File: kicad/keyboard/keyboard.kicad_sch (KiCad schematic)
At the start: 101 parts, among them U3 ATmega328-P, Y1 Crystal

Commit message: Dual support for ASM & C programs. Took some time!
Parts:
- added R1: 5K, Resistor_THT:R_Axial_DIN0204_L3.6mm_D1.6mm_P2.54mm_Vertical, symbol Device:R
- renumbered C4 to C1, C4 to C2, C4 to C3, KD1 to D1, KD10 to D10, KD11 to D11, KD12 to D12, KD13 to D13, KD14 to D14, KD15 to D15, KD16 to D16, KD17 to D17, KD18 to D18, KD19 to D19, KD2 to D2, KD20 to D20, KD21 to D21, KD22 to D22, KD23 to D23, KD24 to D24, KD25 to D25, KD26 to D26, KD27 to D27, KD28 to D28, KD29 to D29, KD3 to D3, KD30 to D30, KD31 to D31, KD32 to D32, KD33 to D33, KD34 to D34, KD35 to D35, KD36 to D36, KD37 to D37, KD38 to D38, KD39 to D39, KD4 to D4, KD40 to D40, KD41 to D41, KD42 to D42, KD43 to D43, KD44 to D44, KD45 to D45, KD46 to D46, KD47 to D47, KD48 to D48, KD5 to D5, KD6 to D6, KD7 to D7, KD8 to D8, KD9 to D9, KSW1 to SW1, KSW10 to SW10, KSW11 to SW11, KSW12 to SW12, KSW13 to SW13, KSW14 to SW14, KSW15 to SW15, KSW16 to SW16, KSW17 to SW17, KSW18 to SW18, KSW19 to SW19, KSW2 to SW2, KSW20 to SW20, KSW21 to SW21, KSW22 to SW22, KSW23 to SW23, KSW24 to SW24, KSW25 to SW25, KSW26 to SW26, KSW27 to SW27, KSW28 to SW28, KSW29 to SW29, KSW3 to SW3, KSW30 to SW30, KSW31 to SW31, KSW32 to SW32, KSW33 to SW33, KSW34 to SW34, KSW35 to SW35, KSW36 to SW36, KSW37 to SW37, KSW38 to SW38, KSW39 to SW39, KSW4 to SW4, KSW40 to SW40, KSW41 to SW41, KSW42 to SW42, KSW43 to SW43, KSW44 to SW44, KSW45 to SW45, KSW46 to SW46, KSW47 to SW47, KSW48 to SW48, KSW5 to SW5, KSW6 to SW6, KSW7 to SW7, KSW8 to SW8, KSW9 to SW9
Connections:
- net +5V: now also R1.2
- net ~{RES}: no longer names the net of U3.1 (~{RESET}/PC6)
- net ~{RES}: now also R1.1

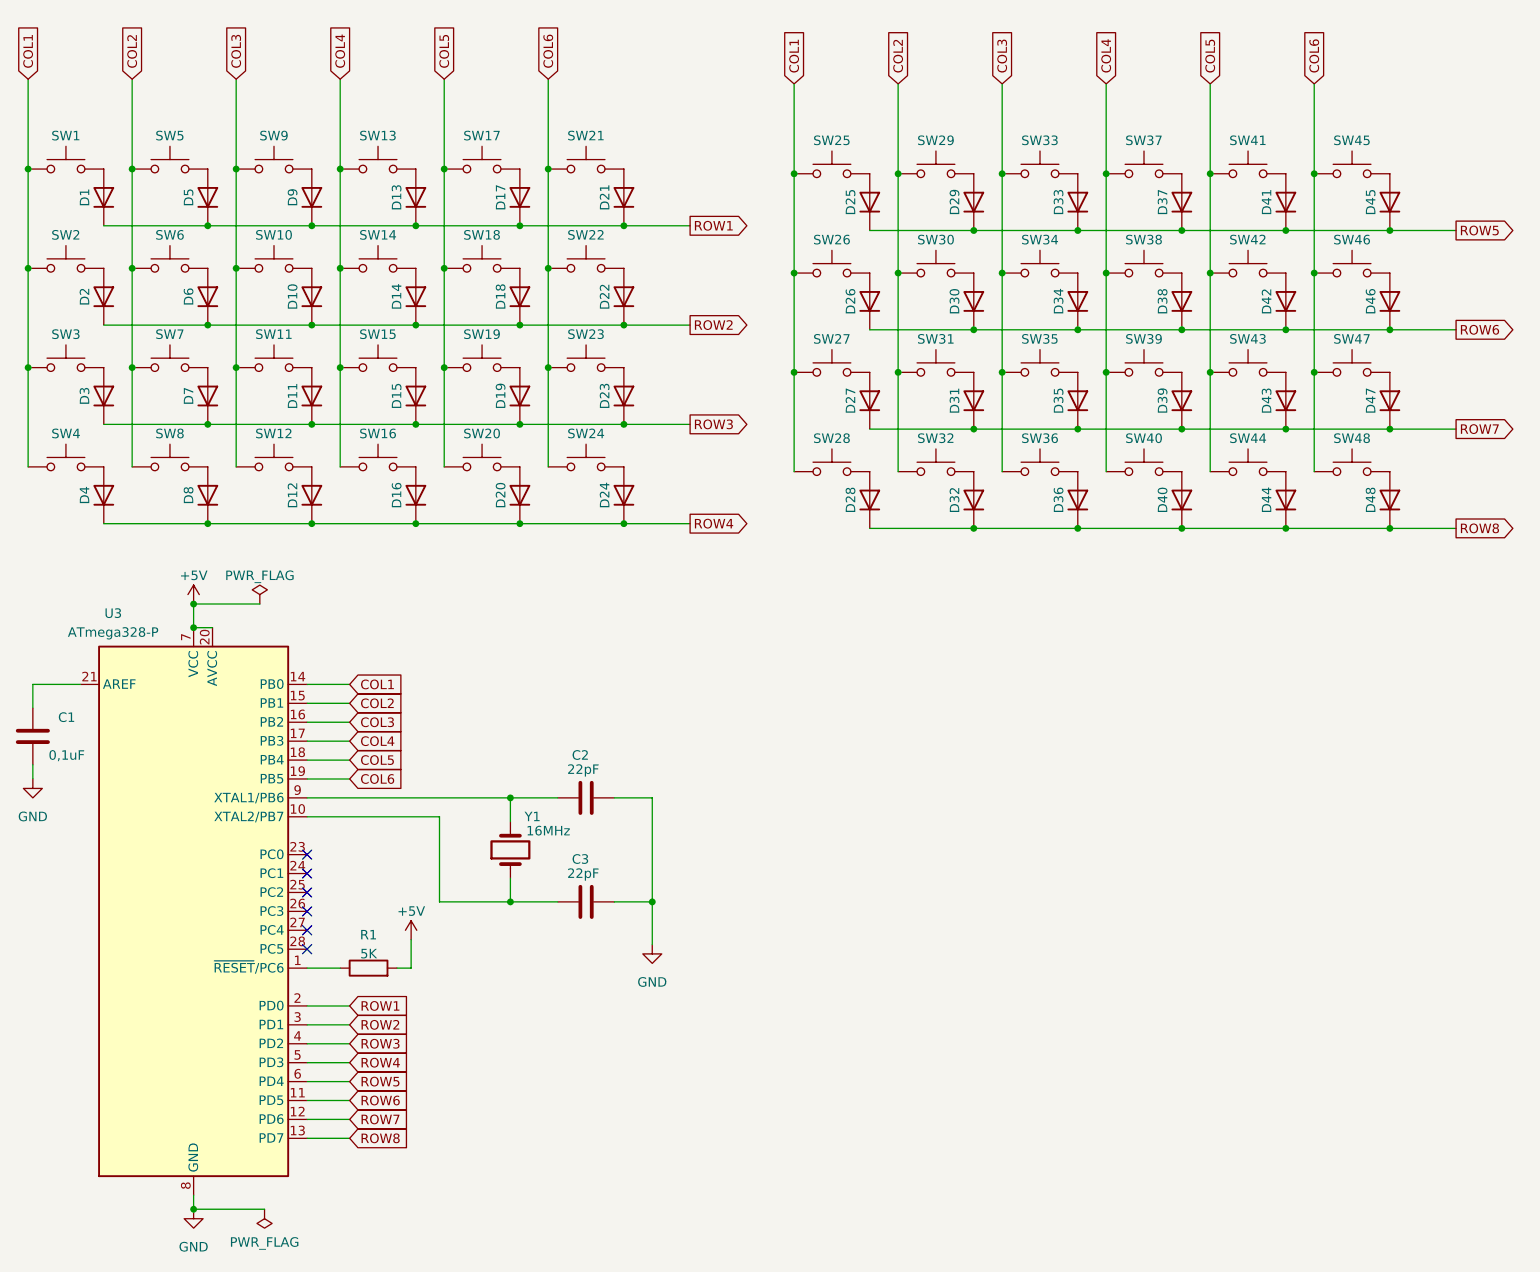
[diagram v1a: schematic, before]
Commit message: Load large files from FAT16, WIP for Maze
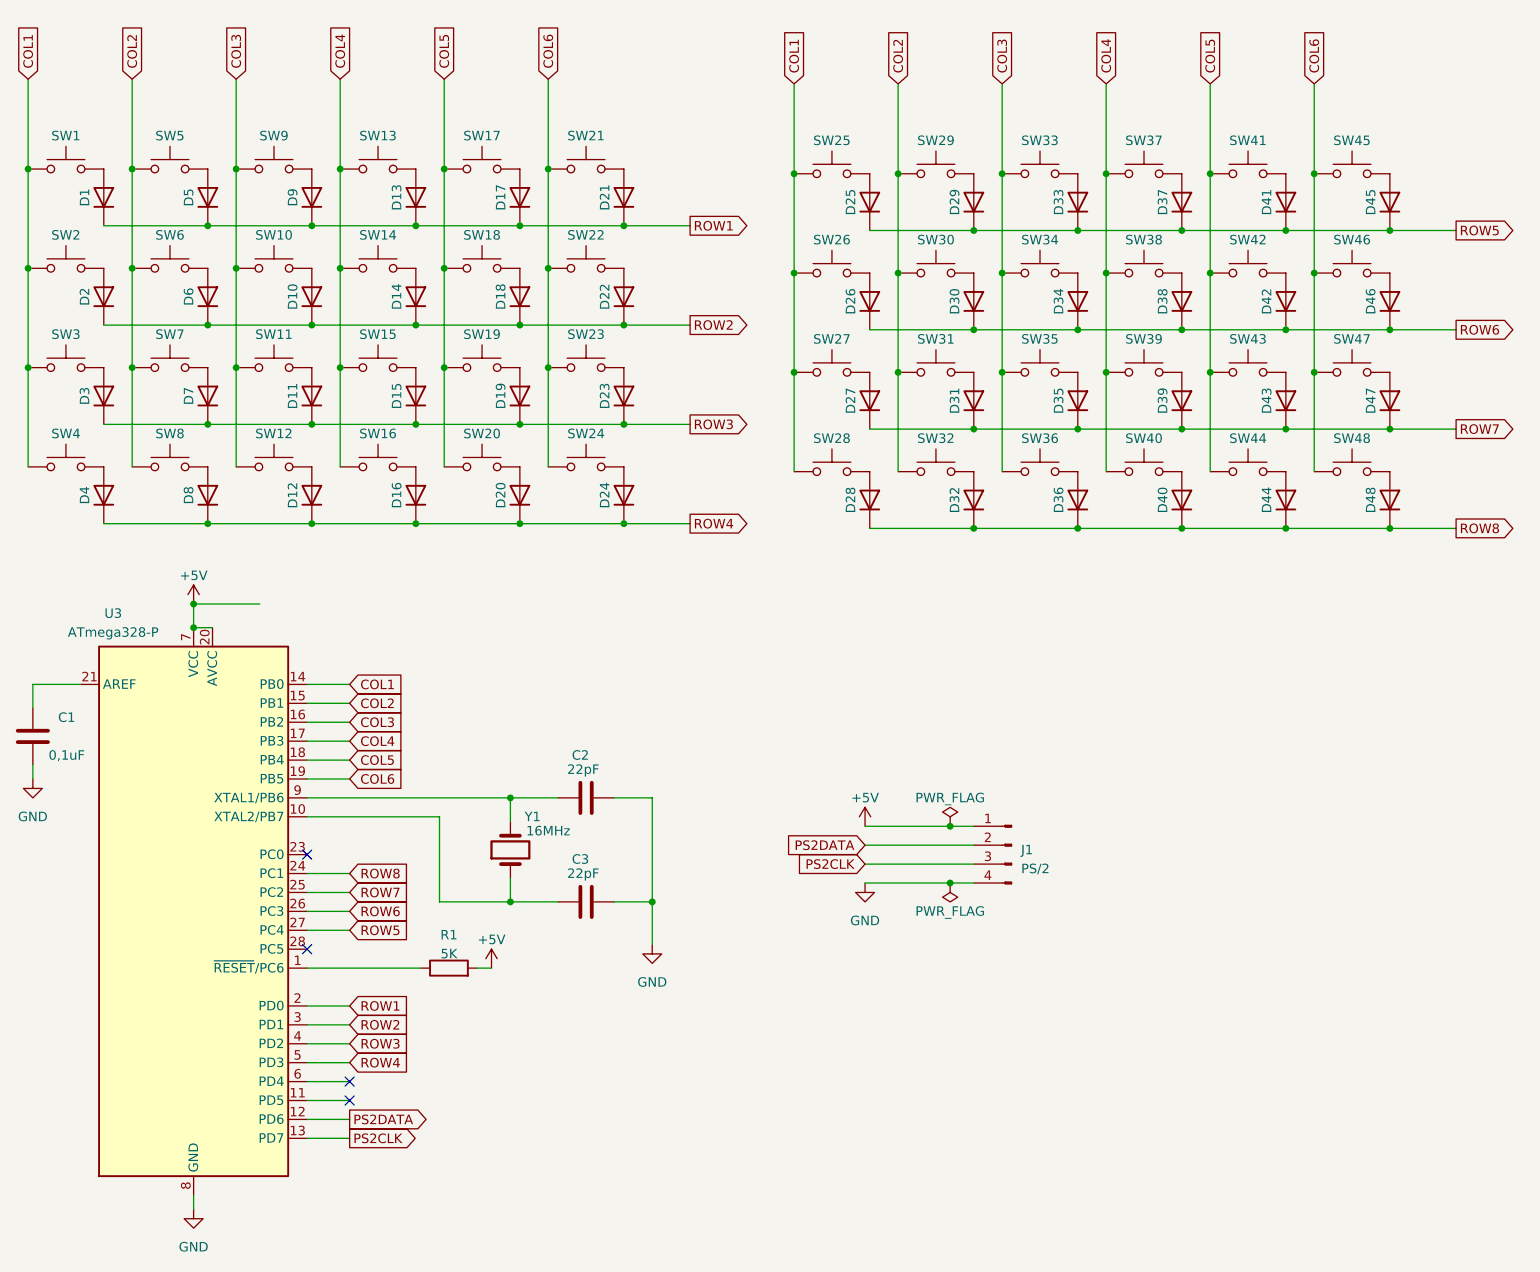
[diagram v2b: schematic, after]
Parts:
- added J1: PS/2, Connector_PinHeader_2.54mm:PinHeader_1x04_P2.54mm_Vertical, symbol Connector:Conn_01x04_Pin
- U3: footprint Package_DIP:DIP-28_W7.62mm -> Package_DIP:DIP-28_W7.62mm_Socket
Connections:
- net +5V: now also J1.1 (Pin_1)
- net GND: now also J1.4 (Pin_4)
- net ROW5: now also U3.27 (PC4); no longer U3.6 (PD4)
- net ROW6: now also U3.26 (PC3); no longer U3.11 (PD5)
- net ROW7: now also U3.25 (PC2); no longer U3.12 (PD6)
- net ROW8: now also U3.24 (PC1); no longer U3.13 (PD7)
- new net PS2CLK: J1.3 (Pin_3), U3.13 (PD7)
- new net PS2DATA: J1.2 (Pin_2), U3.12 (PD6)
- no-connect marks 6 -> 4
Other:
- moved on the sheet: R1
